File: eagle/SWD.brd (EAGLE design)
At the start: 216.4 x 203.2 mm, 69 parts, among them IC1 FT231X, J1 POWER_JACKPTH, U1 OPENMV3-JIG, U2 OPENMV3-JIG, U2-32KB EEPROM-I2CSMD, U3 OPENMV3-JIG, U4 OPENMV3-JIG, U5 OPENMV3-JIG, X1 USB-MICROB, Y1 5MHz-20pF-30ppm

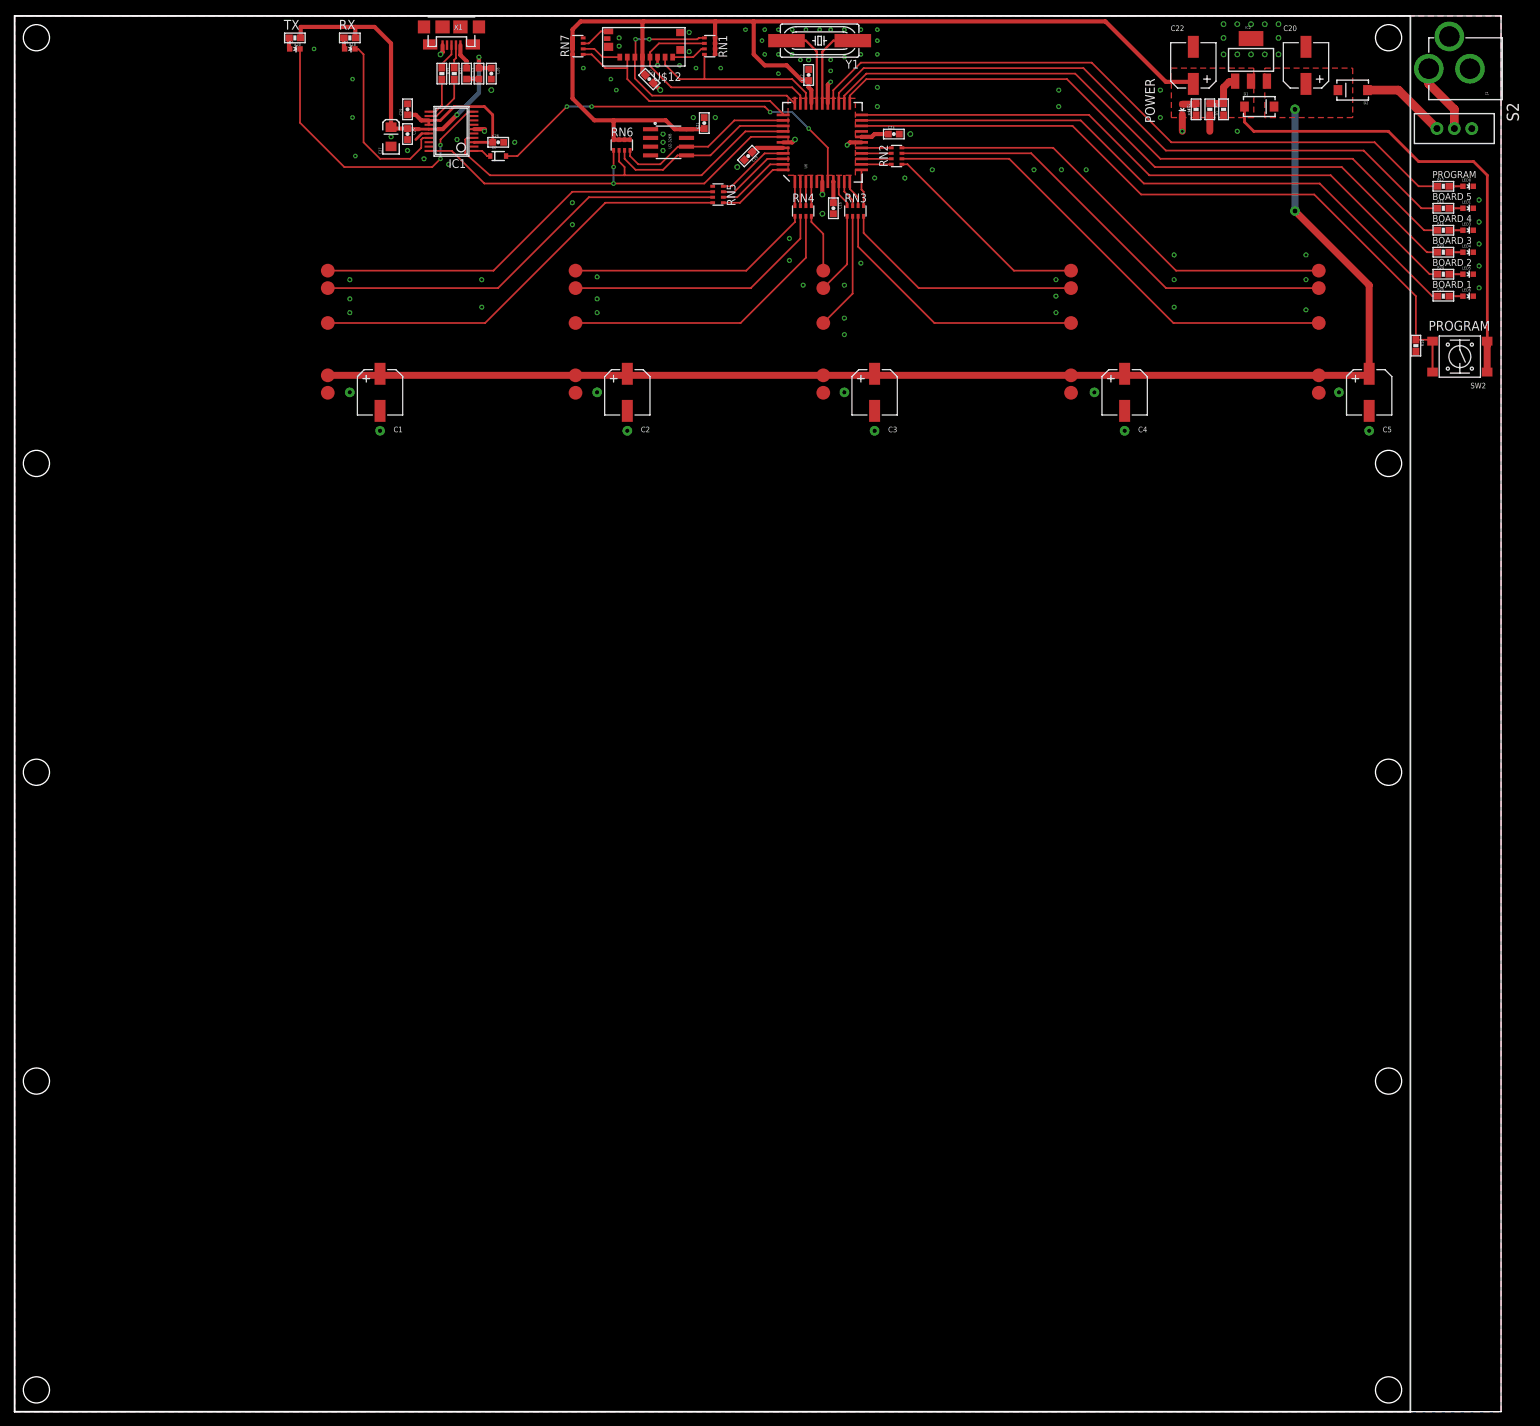
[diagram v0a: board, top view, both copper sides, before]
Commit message: * Update jig (see details)
* Make SWD resistors 100 ohms (RN5-RN2)
* Remove D1 (not really needed).
* Add propeller reset circuit.
* Change all pull-up resistors to 10K.
* Add more silkscreen labels (power switch, power LED, 5V input).
* Use different colors for the power LED, program LED, and board LEDs.
* Add jig instructions to the silk screen.
* Move power LED to be visible.
* Remove FT231x and use FTDI cable header.
* Terminate propeller TX.
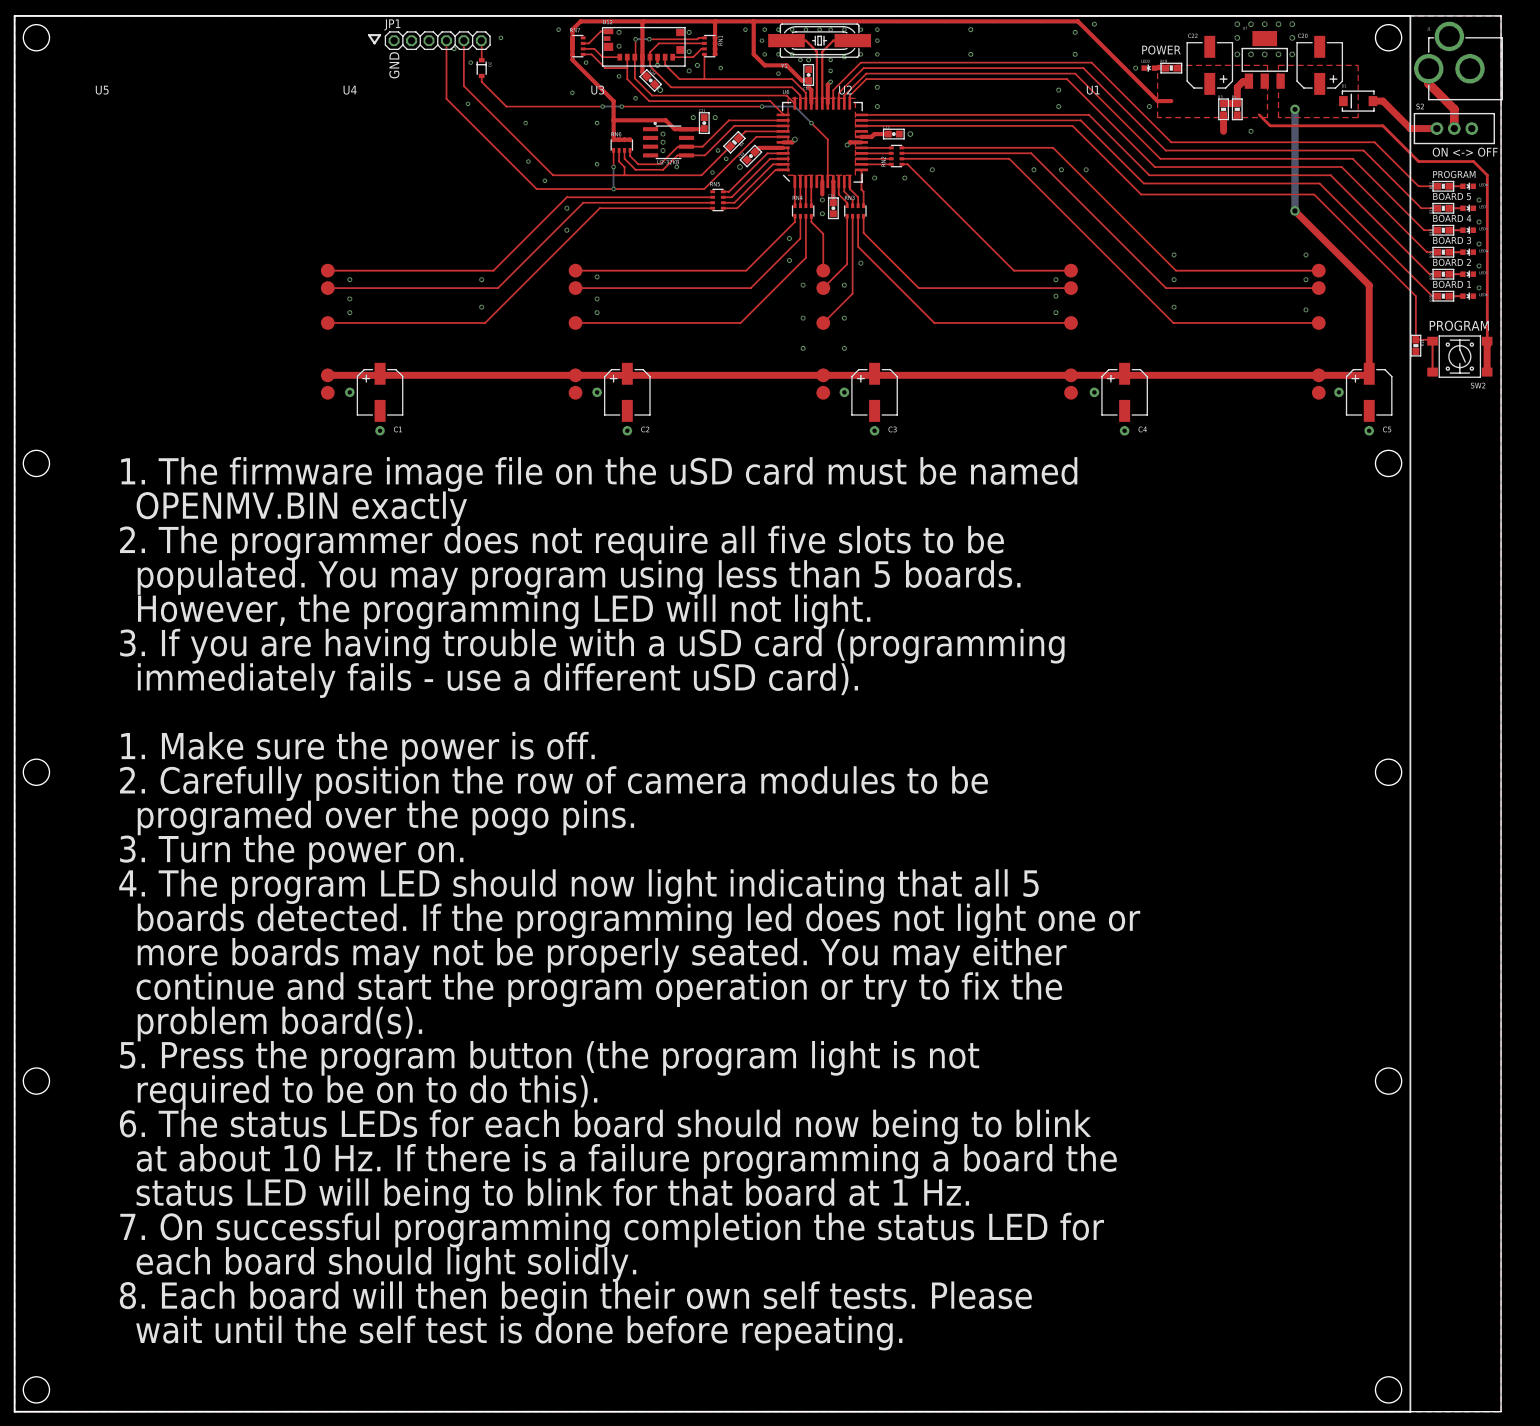
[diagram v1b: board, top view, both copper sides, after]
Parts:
- removed C25, C26, C29: 0.1uF, sfe:0603-CAP
- removed C27: 10uF, sfe:EIA3216
- removed C28: 10nF, sfe:0603-CAP
- removed D5, D6: (no value), sfe:LED-0603
- removed D7: (no value), sfe:SOD-323
- removed F1: PTC0603, sfe:0603
- removed IC1: FT231X, iofault:SSOP20
- removed IC2: (no value), sfe:SOT223
- removed L1: (no value), sfe:0603
- removed R18, R20: 220, sfe:0603-RES
- removed R21, R22: 27R, sfe:0603-RES
- removed X1: USB-MICROB, sfe:USB-MICROB
- added JP1: (no value), pinhead:1X06
- added R4: 100R, sfe:0603-RES
- added U7: (no value), sfe:SOT223
- D2: device sfe:SMA-DIODE -> sfe:SOD-323
- LED1, LED3, LED4, LED5, LED6: value (none) -> GREEN
- LED2, LED8: value (none) -> RED
- R14, RN1, RN6, RN7: value 4.7K -> 10K
- RN2, RN3, RN4, RN5: value 50R -> 100R
- Y1: value 5MHz-20pF-30ppm -> 5MHz-18pF-30ppm
- moved D2 126.8 mm to (68.0, 195.6), turned to 270 degrees
- moved D1 14.4 mm to (195.6, 190.8), turned to 180 degrees
- moved LED2 7.68 mm to (165.2, 195.6), turned to 90 degrees
- moved R19 7.00 mm to (168.4, 195.6), turned to 180 degrees
- moved C22 2.40 mm to (174.0, 196.0)
- moved C20 2.00 mm to (190.0, 196.0)
- moved R1 2.00 mm to (178.0, 189.6)
- moved R3 2.00 mm to (176.0, 189.6)
- moved RN5 0.80 mm to (102.4, 176.4)
- moved C19 0.40 mm to (107.2, 182.8)
- moved C24 0.28 mm to (92.6, 193.8)
- renumbered U$12 to U12
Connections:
- removed net 3V3: C26.1, C29.1, IC1.13, IC1.14, IC1.3
- removed net CTS: IC1.9
- removed net DTR: D7.1, IC1.1
- removed net N$10: R22.1, X1.D+
- removed net N$11: F1.1, L1.2
- removed net N$17: D5.A, R18.2
- removed net N$8: R21.1, X1.D-
- removed net RXLED: D5.C, IC1.17
- removed net TXLED: D6.C, IC1.10
- removed net USBDM: IC1.12, R21.2
- removed net USBDP: IC1.11, R22.2
- removed net VBUS: C25.1, C27.A, C28.1, F1.2, IC1.15, R18.1, R20.1
- removed net VBUS_RAW: L1.1, X1.VBUS
- new net N$1: R4.1, U6.37
- net 3.3V: now also U7.2; no longer D1.A, IC2.2
- net GND: now also JP1.1, U7.4; no longer C25.2, C26.2, C27.C, C28.2, C29.2, IC1.16, IC1.6, IC2.4, X1.GND
- net N$2: now also D1.A; no longer D2.A
- net N$31: now also U7.1; no longer IC2.1
- net N$7: now also D2.2, U6.7; no longer D6.A, R20.2
- net PROP_RESET: now also D2.1, JP1.6; no longer D7.2, U6.7
- net SERIAL_RX: now also JP1.4; no longer IC1.20
- net SERIAL_TX: now also JP1.5, R4.2; no longer IC1.4, U6.37
- net VIN: now also U7.3; no longer D2.C, IC2.3
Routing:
- net N$7: track 1.64 -> 60.8 mm, vias 0 -> 4
- net PROP_RESET: track 57.2 -> 2.87 mm, vias 4 -> 0
- net VBUS: track 53.3 -> 0.00 mm, vias 2 -> 0
- net TXLED: track 43.8 -> 0.00 mm, vias 2 -> 0
- net RXLED: track 26.8 -> 0.00 mm
- net 3V3: track 21.4 -> 0.00 mm
- net SERIAL_RX: track 61.2 -> 71.7 mm
- net GND: track 22.1 -> 14.0 mm, vias 127 -> 135
- net 3.3V: track 245.4 -> 237.5 mm
- net USBDM: track 7.52 -> 0.00 mm
- net N$1: track 0.00 -> 6.90 mm
- net USBDP: track 6.04 -> 0.00 mm
- net N$10: track 3.88 -> 0.00 mm
- net VBUS_RAW: track 3.72 -> 0.00 mm
- net N$8: track 3.40 -> 0.00 mm
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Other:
- board text added: "1. Make sure the power is off."
- board text added: "1. The firmware image file on the uSD card must be named"
- board text added: "2. Carefully position the row of camera modules to be"
- board text added: "2. The programmer does not require all five slots to be"
- board text added: "3. If you are having trouble with a uSD card (programming"
- board text added: "3. Turn the power on."
- board text added: "4. The program LED should now light indicating that all 5"
- board text added: "5. Press the program button (the program light is not"
- board text added: "6. The status LEDs for each board should now being to blink"
- board text added: "7. On successful programming completion the status LED for"
- board text added: "8. Each board will then begin their own self tests. Please"
- board text added: "GND"
- board text added: "However, the programming LED will not light."
- board text added: "ON <-> OFF"
- board text added: "OPENMV.BIN exactly"
- board text added: "at about 10 Hz. If there is a failure programming a board the"
- board text added: "boards detected. If the programming led does not light one or"
- board text added: "continue and start the program operation or try to fix the"
- board text added: "each board should light solidly."
- board text added: "immediately fails - use a different uSD card)."
- board text added: "more boards may not be properly seated. You may either"
- board text added: "populated. You may program using less than 5 boards."
- board text added: "problem board(s)."
- board text added: "programed over the pogo pins."
- board text added: "required to be on to do this)."
- board text added: "status LED will being to blink for that board at 1 Hz."
- board text added: "wait until the self test is done before repeating."
- board text removed: "RX"
- board text removed: "TX"

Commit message: Replace common parts with MF parts
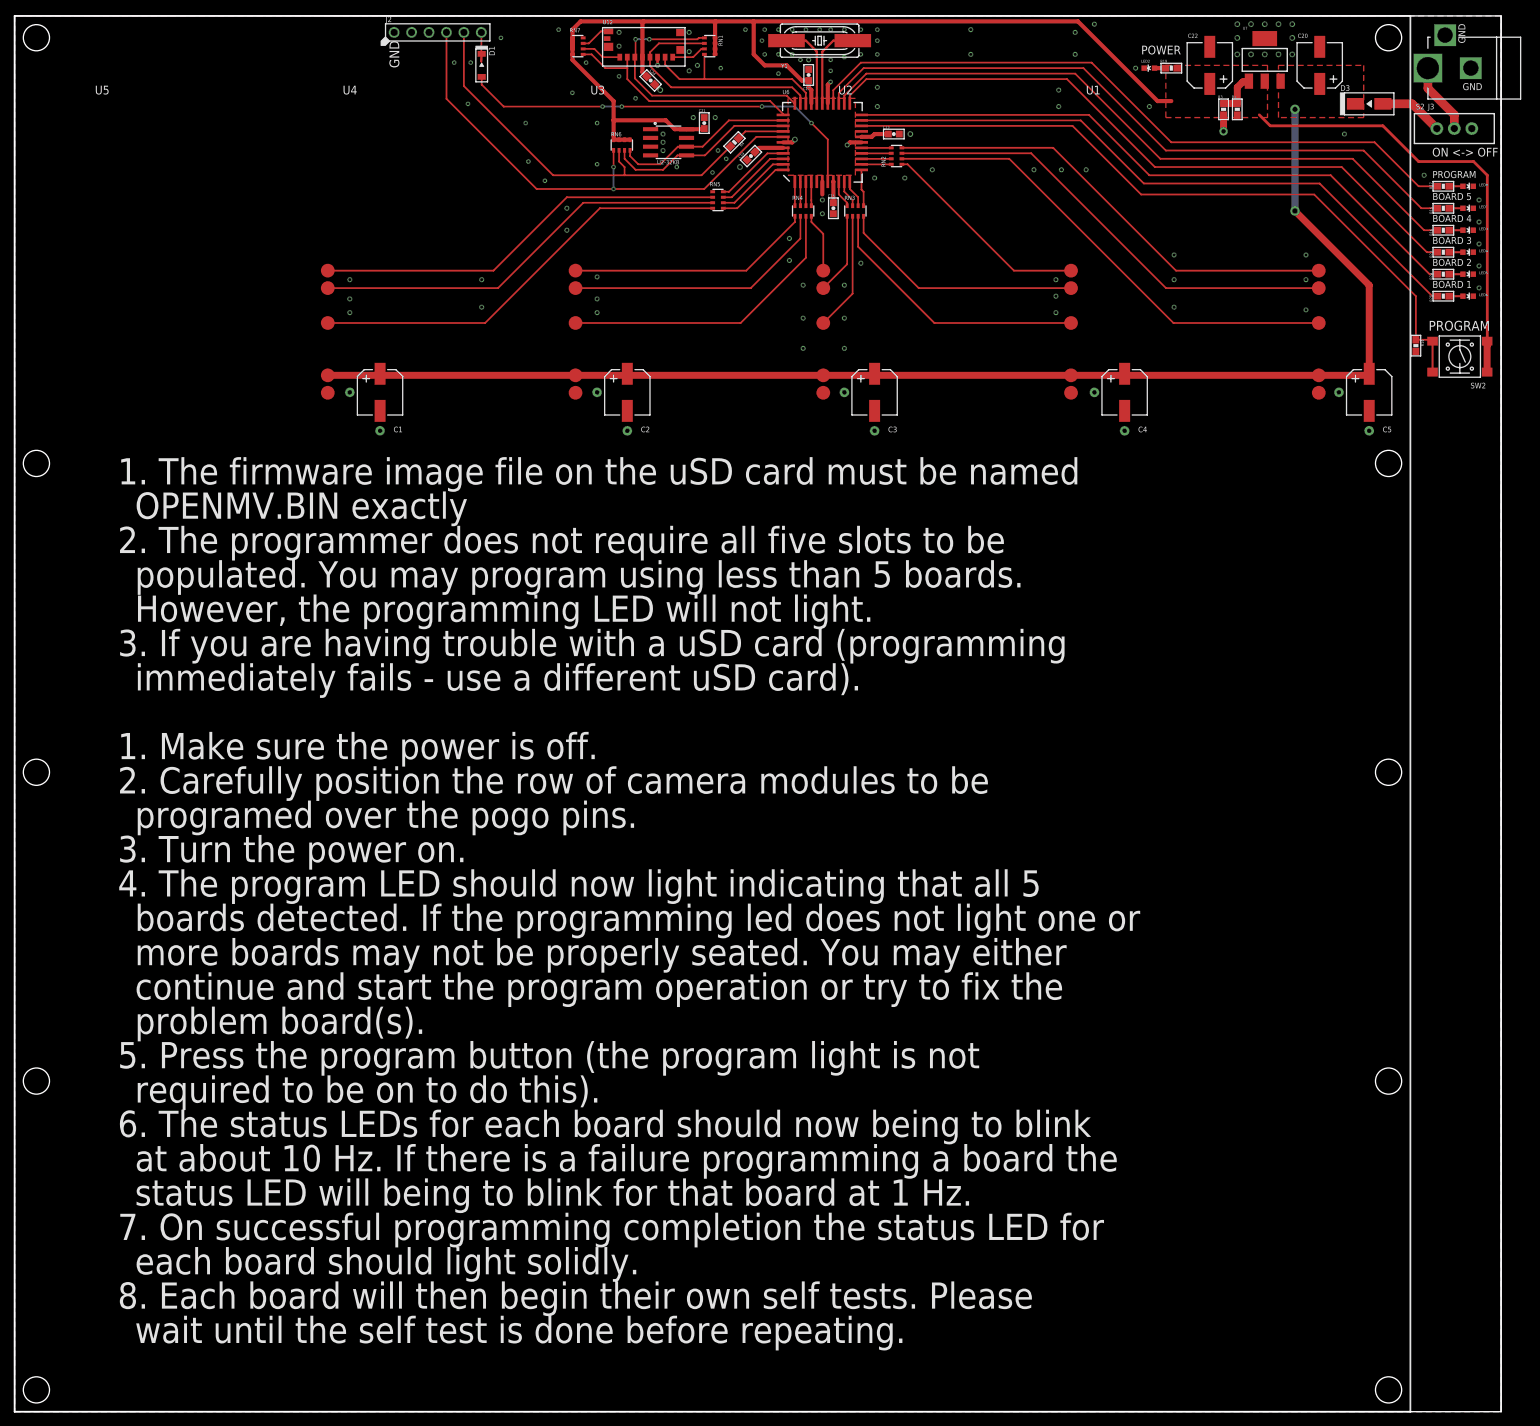
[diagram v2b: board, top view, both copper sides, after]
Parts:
- removed D2: (no value), sfe:SOD-323
- removed J1: POWER_JACKPTH, sfe:POWER_JACK_PTH
- removed JP1: (no value), pinhead:1X06
- added D3: (no value), MF_Discrete_Semiconductor:SMA
- added J2: (no value), MF_Connectors:PTH_2.54MM_01X06
- added J3: (no value), MF_Connectors:DC_PWR_JACK
- D1: device sfe:SMA-DIODE -> MF_Discrete_Semiconductor:SOD-123
- moved D1 127.7 mm to (68.0, 196.0), turned to 270 degrees
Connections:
- net GND: now also J2.P$1, J3.SLEEVE1, J3.SLEEVE2; no longer J1.GND, J1.GNDBREAK, JP1.1
- net N$2: now also D3.ANODE; no longer D1.A
- net N$7: now also D1.ANODE; no longer D2.2
- net N$9: now also J3.PIN; no longer J1.PWR
- net PROP_RESET: now also D1.CATHODE, J2.P$6; no longer D2.1, JP1.6
- net SERIAL_RX: now also J2.P$4; no longer JP1.4
- net SERIAL_TX: now also J2.P$5; no longer JP1.5
- net VIN: now also D3.CATHODE; no longer D1.C
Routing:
- net PROP_RESET: track 2.87 -> 5.43 mm
- net N$2: track 11.0 -> 9.35 mm
- net SERIAL_TX: track 56.5 -> 57.7 mm
- net SERIAL_RX: track 71.7 -> 72.9 mm
- net GND: vias 135 -> 137
